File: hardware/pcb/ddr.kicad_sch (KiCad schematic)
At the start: 6 parts, among them U2 K4E8E324EB-EGCF

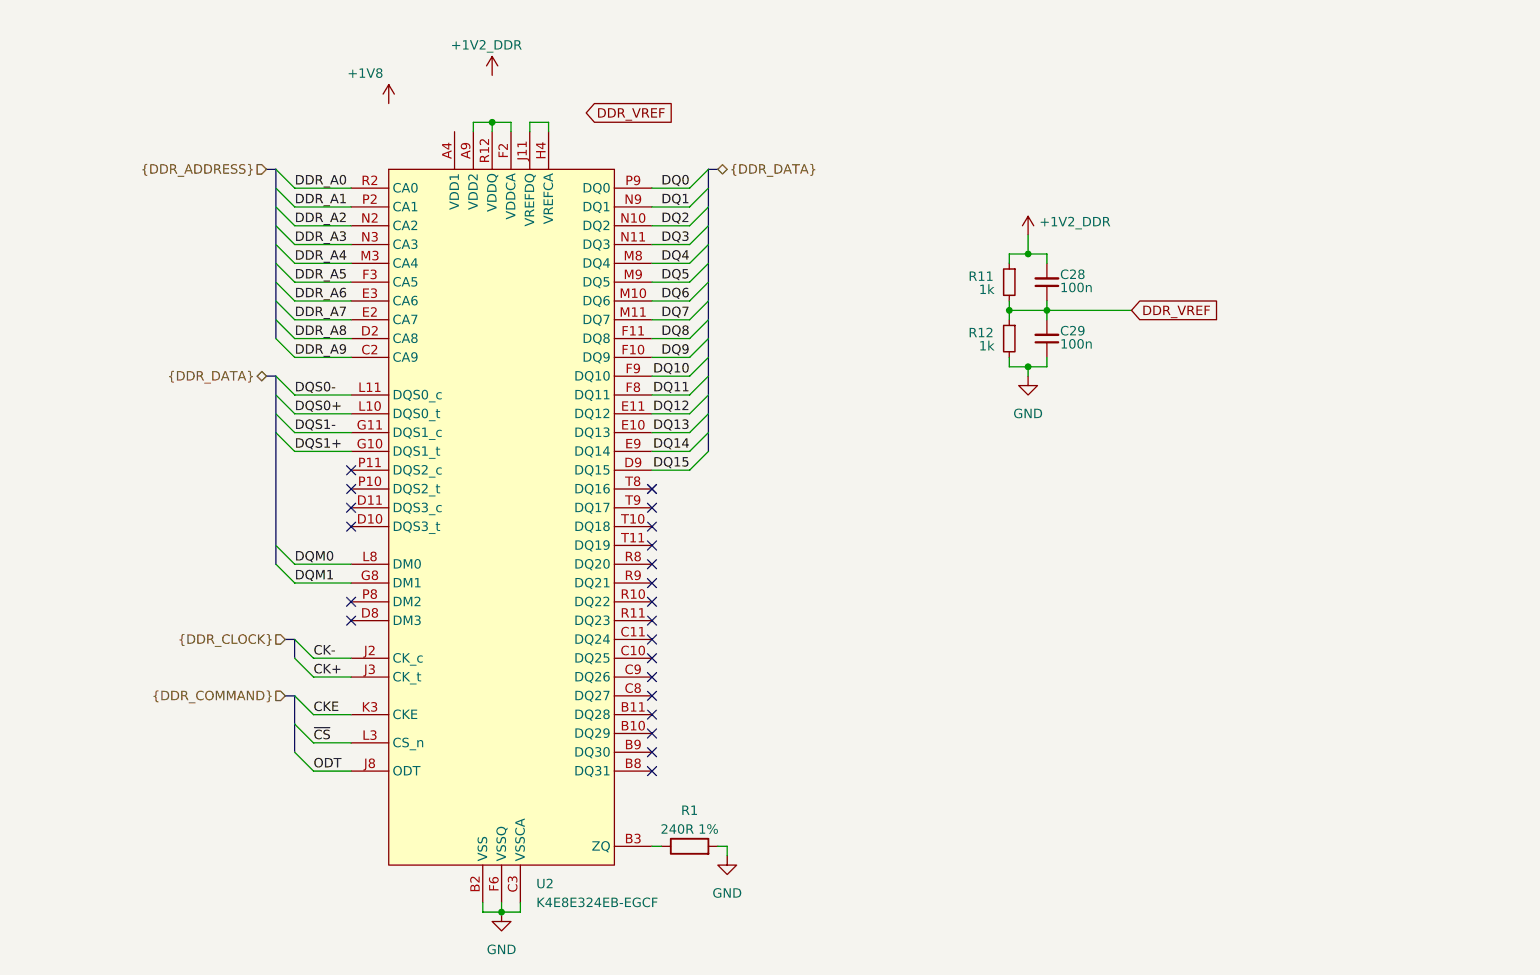
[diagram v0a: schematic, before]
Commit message: replaced lpddr3 with ddr3l
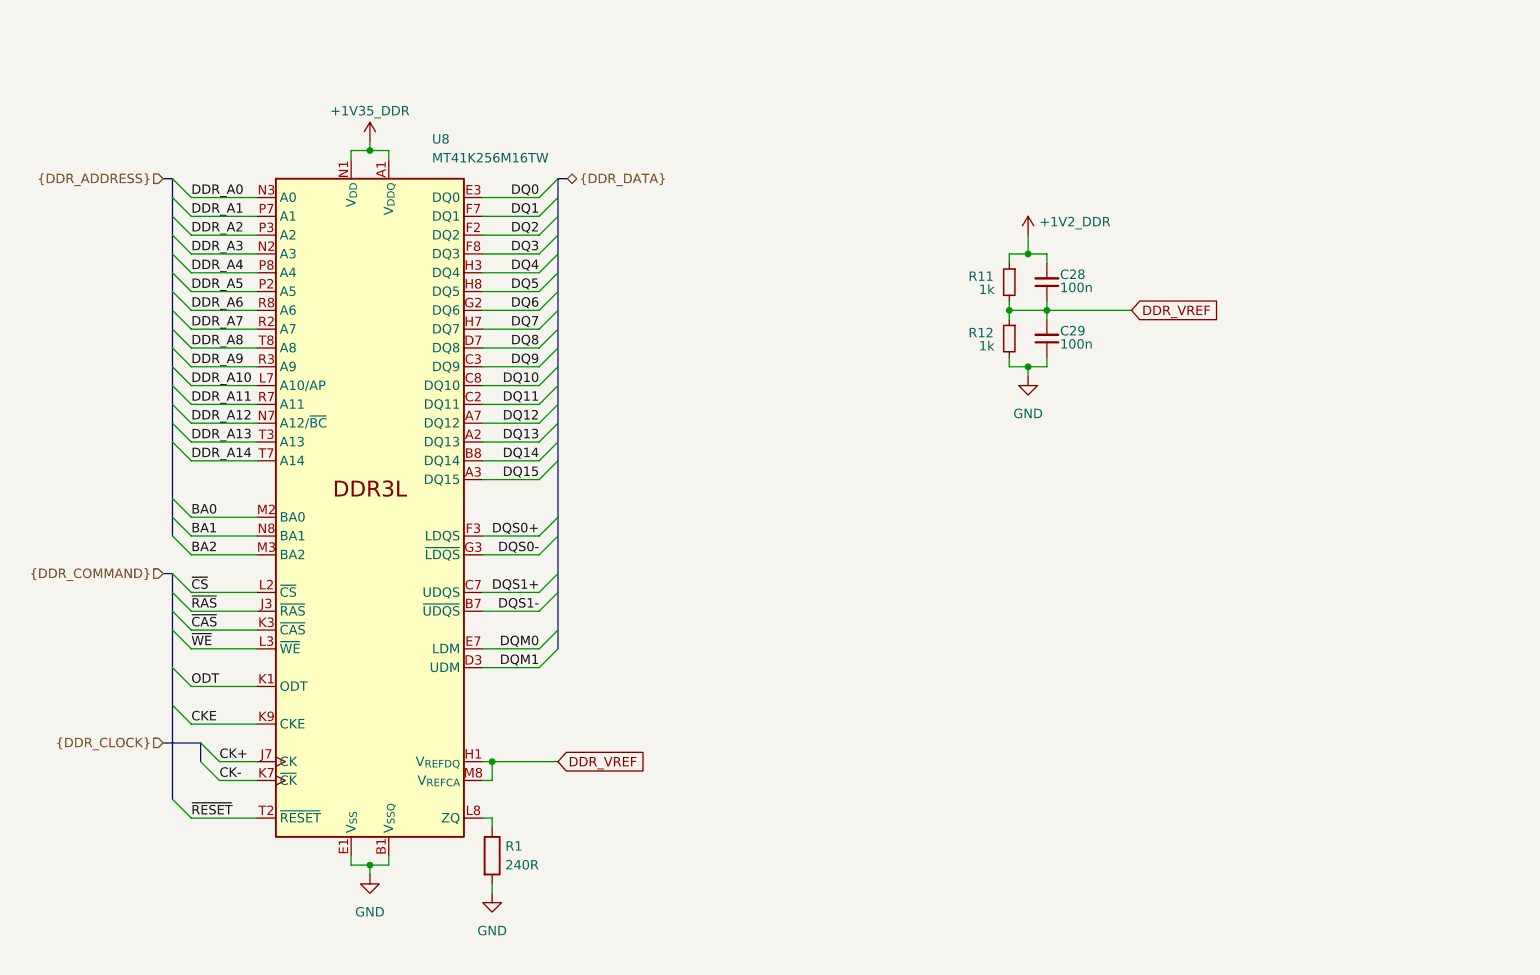
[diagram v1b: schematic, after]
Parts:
- removed U2: K4E8E324EB-EGCF, K4E6E304EC-EGCG:FBGA-178_L11.5-W11.0_K4E6E304EC-TL, symbol K4E6E304EC-EGCG:K4E8E324EB-EGCF
- added U8: MT41K256M16TW, Package_BGA:Micron_FBGA-96_8x14mm_Layout9x16_P0.8mm, symbol Memory_RAM:MT41K256M16TW
- R1: value 240R 1% -> 240R
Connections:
- net CK+: now also U8.J7 (CK)
- net CK-: now also U8.K7 (~{CK})
- net CKE: now also U8.K9 (CKE)
- net DDR_A0: now also U8.N3 (A0)
- net DDR_A1: now also U8.P7 (A1)
- net DDR_A2: now also U8.P3 (A2)
- net DDR_A3: now also U8.N2 (A3)
- net DDR_A4: now also U8.P8 (A4)
- net DDR_A5: now also U8.P2 (A5)
- net DDR_A6: now also U8.R8 (A6)
- net DDR_A7: now also U8.R2 (A7)
- net DDR_A8: now also U8.T8 (A8)
- net DDR_A9: now also U8.R3 (A9)
- net DDR_VREF: now also U8.H1 (V_{REFDQ}), U8.M8 (V_{REFCA})
- net DQ0: now also U8.E3 (DQ0)
- net DQ1: now also U8.F7 (DQ1)
- net DQ10: now also U8.C8 (DQ10)
- net DQ11: now also U8.C2 (DQ11)
- net DQ12: now also U8.A7 (DQ12)
- net DQ13: now also U8.A2 (DQ13)
- net DQ14: now also U8.B8 (DQ14)
- net DQ15: now also U8.A3 (DQ15)
- net DQ2: now also U8.F2 (DQ2)
- net DQ3: now also U8.F8 (DQ3)
- net DQ4: now also U8.H3 (DQ4)
- net DQ5: now also U8.H8 (DQ5)
- net DQ6: now also U8.G2 (DQ6)
- net DQ7: now also U8.H7 (DQ7)
- net DQ8: now also U8.D7 (DQ8)
- net DQ9: now also U8.C3 (DQ9)
- net DQM0: now also U8.E7 (LDM)
- net DQM1: now also U8.D3 (UDM)
- net DQS0+: now also U8.F3 (LDQS)
- net DQS0-: now also U8.G3 (~{LDQS})
- net DQS1+: now also U8.C7 (UDQS)
- net DQS1-: now also U8.B7 (~{UDQS})
- net GND: now also U8.A9 (V_{SS}), U8.B1 (V_{SSQ}), U8.B3 (V_{SS}), U8.B9 (V_{SSQ}), U8.D1 (V_{SSQ}), U8.D8 (V_{SSQ}), U8.E1 (V_{SS}), U8.E2 (V_{SSQ}), U8.E8 (V_{SSQ}), U8.F9 (V_{SSQ}), U8.G1 (V_{SSQ}), U8.G8 (V_{SS}), U8.G9 (V_{SSQ}), U8.J2 (V_{SS}), U8.J8 (V_{SS}), U8.M1 (V_{SS}), U8.M9 (V_{SS}), U8.P1 (V_{SS}), U8.P9 (V_{SS}), U8.T1 (V_{SS}), U8.T9 (V_{SS})
- net ODT: now also U8.K1 (ODT)
- net ~{CS}: now also U8.L2 (~{CS})
- net at R1.1: now also U8.L8 (ZQ)
- new net +1V35_DDR: U8.A1 (V_{DDQ}), U8.A8 (V_{DDQ}), U8.B2 (V_{DD}), U8.C1 (V_{DDQ}), U8.C9 (V_{DDQ}), U8.D2 (V_{DDQ}), U8.D9 (V_{DD}), U8.E9 (V_{DDQ}), U8.F1 (V_{DDQ}), U8.G7 (V_{DD}), U8.H2 (V_{DDQ}), U8.H9 (V_{DDQ}), U8.K2 (V_{DD}), U8.K8 (V_{DD}), U8.N1 (V_{DD}), U8.N9 (V_{DD}), U8.R1 (V_{DD}), U8.R9 (V_{DD})
- new net BA0: U8.M2 (BA0)
- new net BA1: U8.N8 (BA1)
- new net BA2: U8.M3 (BA2)
- new net DDR_A10: U8.L7 (A10/AP)
- new net DDR_A11: U8.R7 (A11)
- new net DDR_A12: U8.N7 (A12/~{BC})
- new net DDR_A13: U8.T3 (A13)
- new net DDR_A14: U8.T7 (A14)
- new net ~{CAS}: U8.K3 (~{CAS})
- new net ~{RAS}: U8.J3 (~{RAS})
- new net ~{RESET}: U8.T2 (~{RESET})
- new net ~{WE}: U8.L3 (~{WE})
- no-connect marks 22 -> 0
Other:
- moved on the sheet: R1

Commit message: moved stuff around
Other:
- moved on the sheet: C28, C29, R11, R12

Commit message: assigning pins
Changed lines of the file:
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@@
-	)
-	(global_label "DDR_VREF"
-		(shape output)
-		(at 176.53 76.2 0)
-		(fields_autoplaced yes)
-		(effects
-			(font
-				(size 1.27 1.27)
-			)
-			(justify left)
-		)
-		(property "Intersheetrefs" "${INTERSHEET_REFS}"
-			(at 188.889 76.2 0)
-			(hide yes)
-			(show_name no)
-			(do_not_autoplace no)
-			(effects
-				(font
-					(size 1.27 1.27)
-				)
-				(justify left)
-			)
-		)
 	)
 	(global_label "DDR_VREF"
@@
 		)
 	)
+	(hierarchical_label "DDR_VREF"
+		(shape passive)
+		(at 176.53 76.2 0)
+		(effects
+			(font
+				(size 1.27 1.27)
+			)
+			(justify left)
+		)
+	)

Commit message: looking over stuff, added caps
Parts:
- added C48, C67: 4u7, Capacitor_SMD:C_0402_1005Metric, symbol Device:C_Small
- added C49, C50, C51, C52, C53, C54, C55, C56, C57, C58, C59, C60, C61, C62, C63, C64, C65, C66: 100n, Capacitor_SMD:C_0402_1005Metric, symbol Device:C_Small
- C28, C29: footprint (none) -> Capacitor_SMD:C_0402_1005Metric
- R1, R11, R12: footprint (none) -> Resistor_SMD:R_0402_1005Metric
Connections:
- net +1V2_DDR: now also C48.1
- net +1V35_DDR: now also C49.1, C50.1, C51.1, C52.1, C53.1, C54.1, C55.1, C56.1, C57.1, C58.1, C59.1, C60.1, C61.1, C62.1, C63.1, C64.1, C65.1, C66.1, C67.1
- net GND: now also C48.2, C49.2, C50.2, C51.2, C52.2, C53.2, C54.2, C55.2, C56.2, C57.2, C58.2, C59.2, C60.2, C61.2, C62.2, C63.2, C64.2, C65.2, C66.2, C67.2
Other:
- moved on the sheet: C28, C29, R11, R12

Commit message: started cleaning up schematic
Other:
- company: (none) -> Gensis
- title: (none) -> DDR
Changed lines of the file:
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@@
 	(generator_version "10.0")
 	(paper "A4")
+	(title_block
+		(title "DDR")
+		(rev "v1.0.0")
+		(company "Gensis")
+	)
 	(junction
 		(at 243.84 44.45)

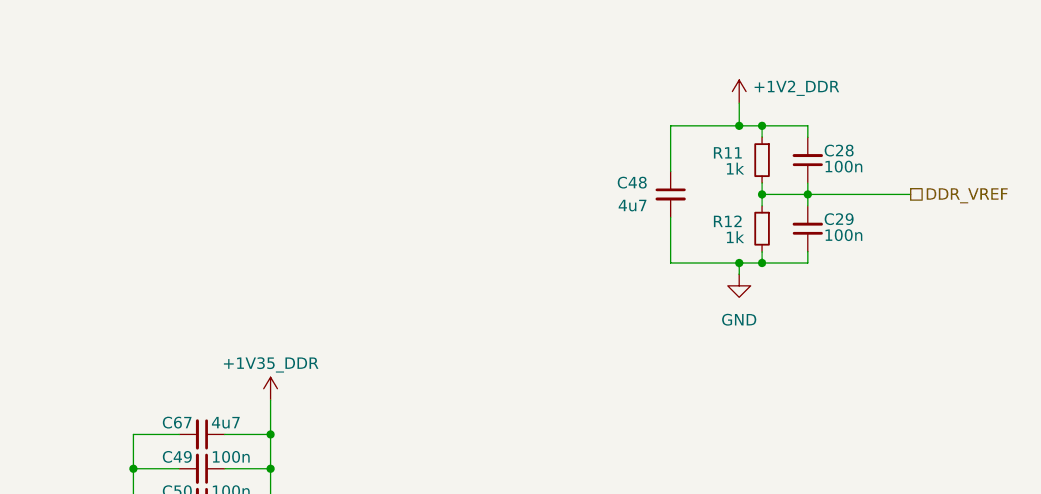
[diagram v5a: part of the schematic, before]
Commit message: main board: fixed schematic errors, made sama7 symbol better
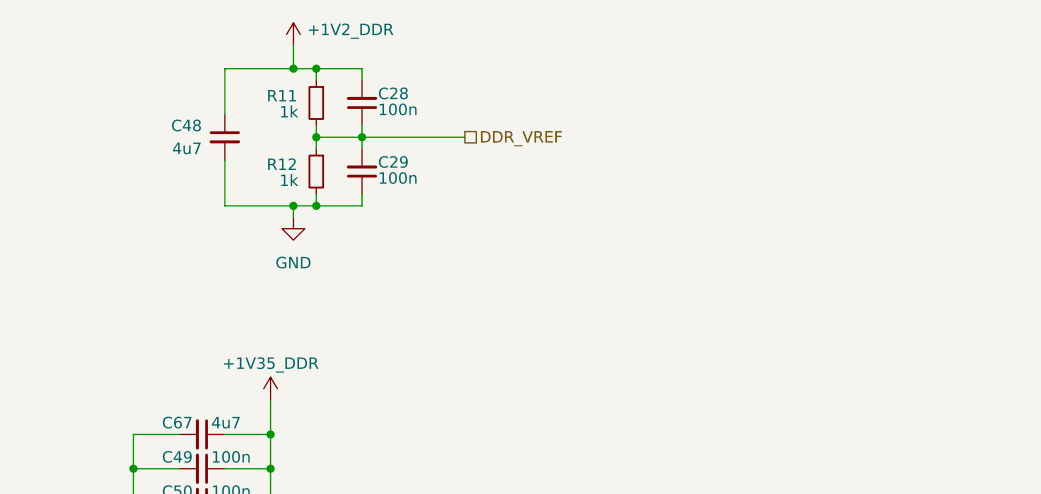
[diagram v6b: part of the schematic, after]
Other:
- moved on the sheet: C28, C29, C48, R11, R12

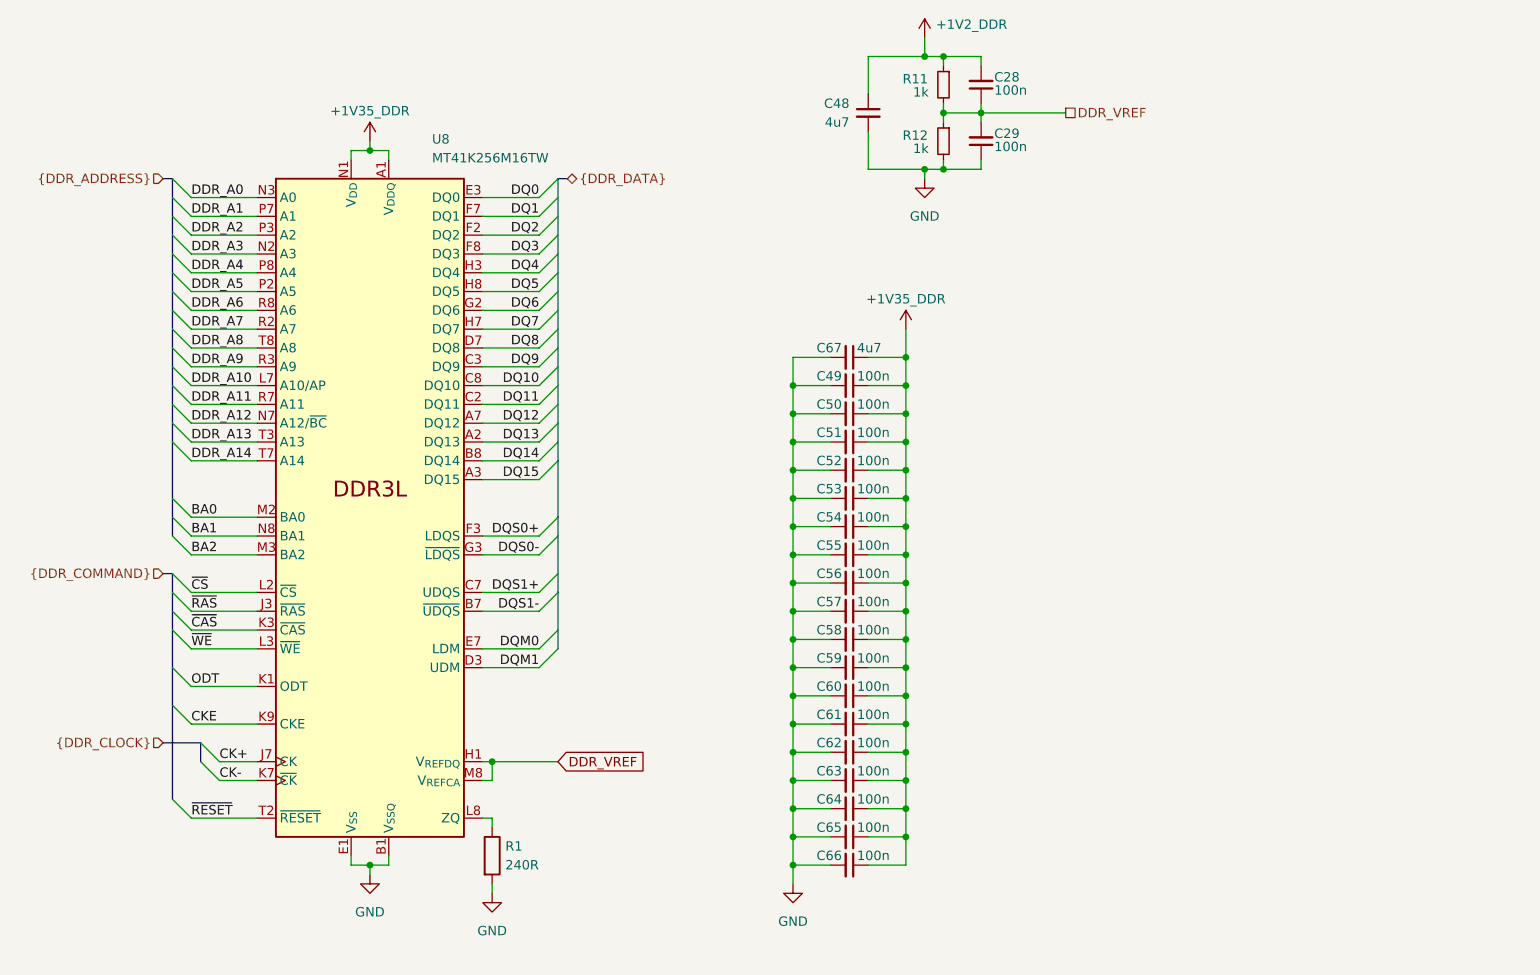
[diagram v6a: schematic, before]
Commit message: mainboard: reannotated schematic
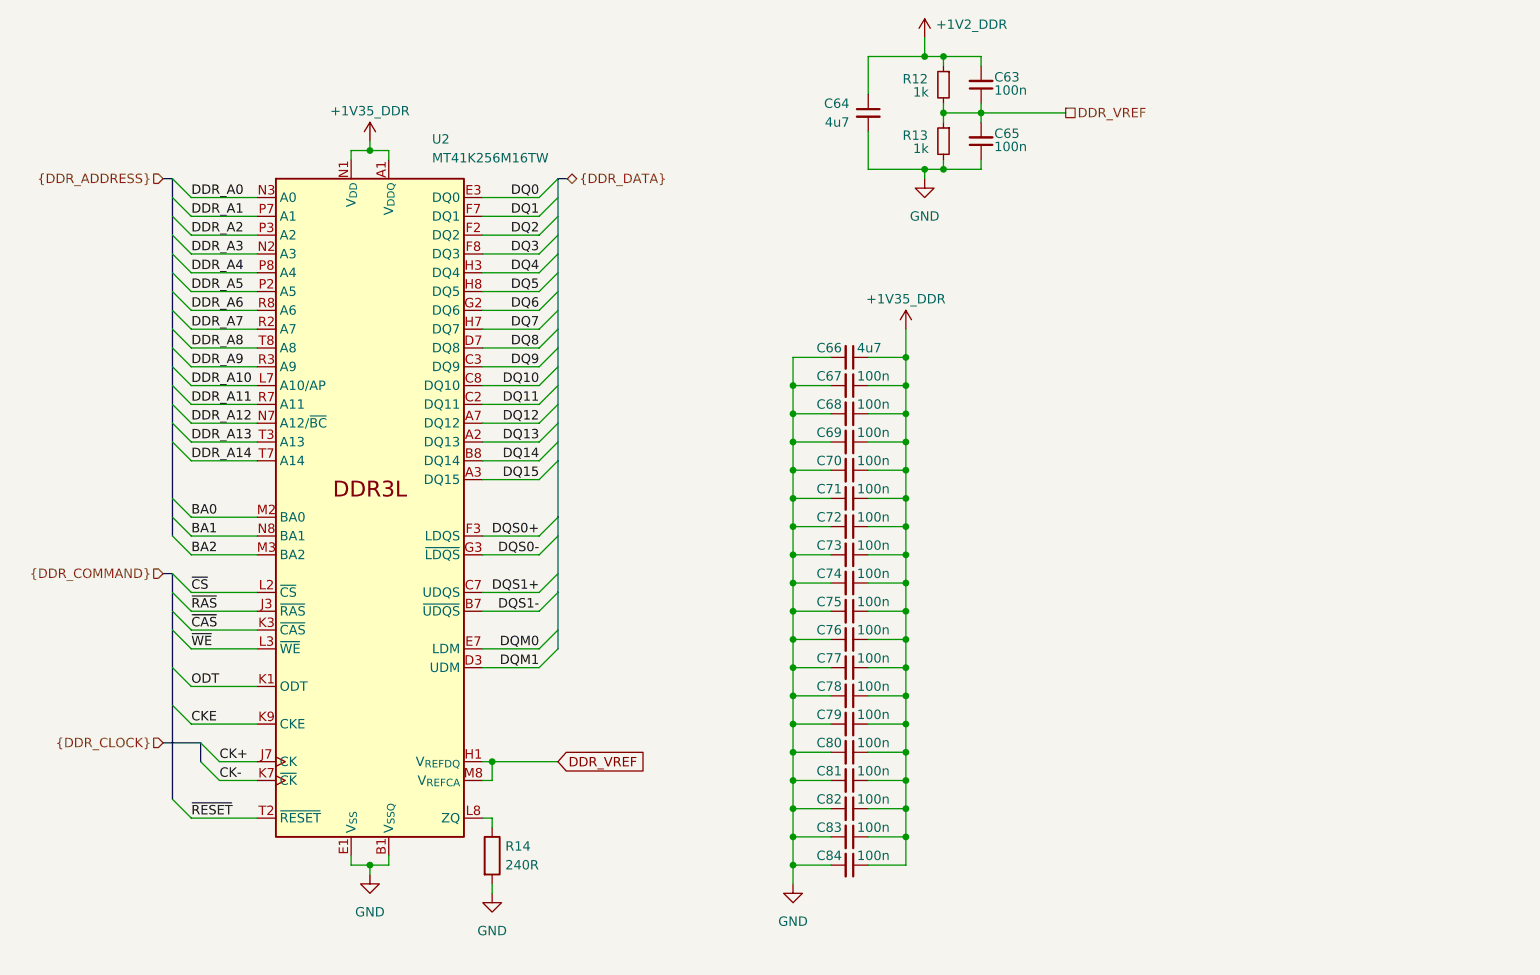
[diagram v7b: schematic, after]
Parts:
- renumbered C28 to C63, C48 to C64, C29 to C65, C67 to C66, C49 to C67, C50 to C68, C51 to C69, C52 to C70, C53 to C71, C54 to C72, C55 to C73, C56 to C74, C57 to C75, C58 to C76, C59 to C77, C60 to C78, C61 to C79, C62 to C80, C63 to C81, C64 to C82, C65 to C83, C66 to C84, R11 to R12, R12 to R13, R1 to R14, U8 to U2
